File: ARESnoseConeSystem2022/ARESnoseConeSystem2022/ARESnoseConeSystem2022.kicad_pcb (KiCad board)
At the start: 2 copper layers, 125.2 x 66 mm, 36 parts, among them J1 436500200, J2 436500200, J3 BMP390_Headers, J4 ICM20948_Headers, J5 GPS_Headers1, J6 Transmitter_Headers1, J7 Conn_01x08, J8 Transmitter_Headers2, U1 L7805, U2 Teensy4.1

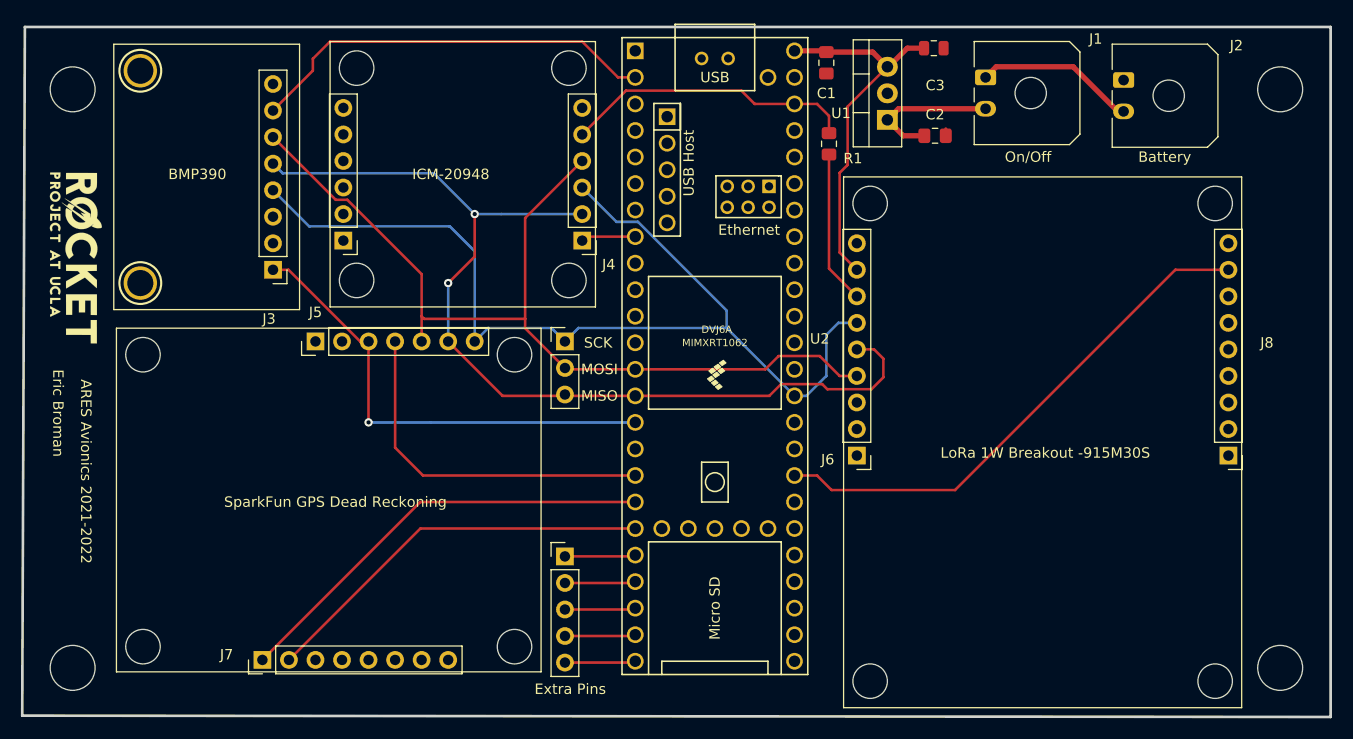
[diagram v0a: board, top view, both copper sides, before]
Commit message: Reworked Power & GND
New regulator + ground planes
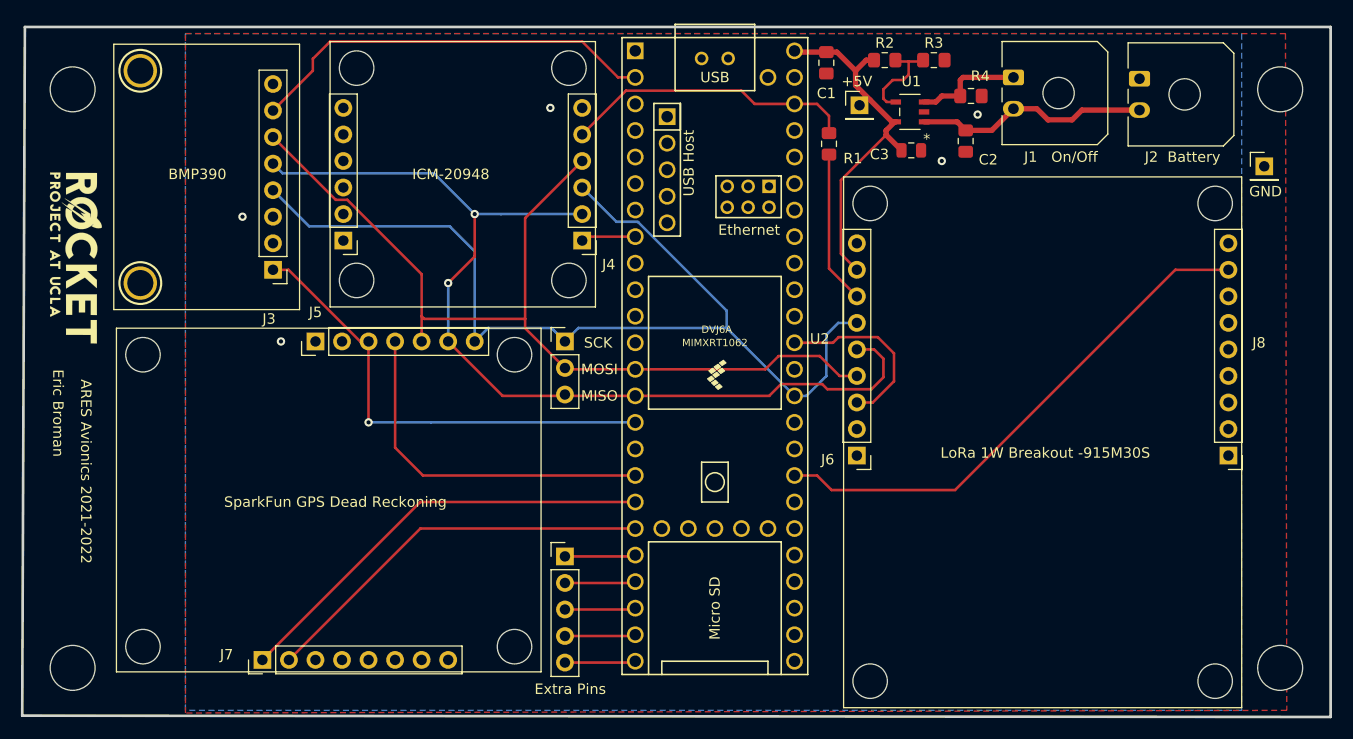
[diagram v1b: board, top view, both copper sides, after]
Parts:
- added +5V: PinHeader_1x01_P2.54mm_Vertical, Connector_PinHeader_2.54mm:PinHeader_1x01_P2.54mm_Vertical, F.Cu at (127.1, 53.7)
- added GND: PinHeader_1x01_P2.54mm_Vertical, Connector_PinHeader_2.54mm:PinHeader_1x01_P2.54mm_Vertical, F.Cu at (165.9, 59.6)
- added R2: 3 kOhm, Resistor_SMD:R_0805_2012Metric_Pad1.15x1.40mm_HandSolder, F.Cu at (129.5, 49.4)
- added R3: 9,1 kOhm, Resistor_SMD:R_0805_2012Metric_Pad1.15x1.40mm_HandSolder, F.Cu at (134.2, 49.4)
- added R4: 10 kOhm, Resistor_SMD:R_0805_2012Metric_Pad1.15x1.40mm_HandSolder, F.Cu at (137.8, 52.8)
- U1: value L7805 -> AP2210K-ADJTRG1; footprint Package_TO_SOT_THT:TO-220-3_Vertical -> footprints:AP2210K-ADJTRG1
- moved C3 10.0 mm to (132.1, 58.0)
- moved C2 2.97 mm to (137.3, 57.1), turned to 270 degrees
- moved J1 2.67 mm to (141.9, 51.1)
- moved U1 2.29 mm to (132.0, 54.4), turned to 180 degrees
- moved J2 1.53 mm to (153.9, 51.2)
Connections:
- C2 pad 1: Net-(C2-Pad1) -> +BATT
- J1 pad 2: Net-(C2-Pad1) -> +BATT
- J2 pad 2: Net-(J1-Pad1) -> +BATT
- U1 pad 1: Net-(C2-Pad1) -> +BATT
- U1 pad 3: 5V -> Net-(J1-Pad1)
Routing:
- net +BATT: track 0.00 -> 22.6 mm
- net /TRANSMITTER_CS: track 0.00 -> 17.5 mm
- net Net-(C2-Pad1): track 14.0 -> 0.00 mm
- net Net-(R2-Pad2): track 0.00 -> 9.22 mm
- net Net-(J1-Pad1): track 15.4 -> 10.4 mm
- net GND: track 0.70 -> 0.00 mm, vias 0 -> 5
- added copper zone on B.Cu, net GND
- added copper zone on F.Cu, net GND

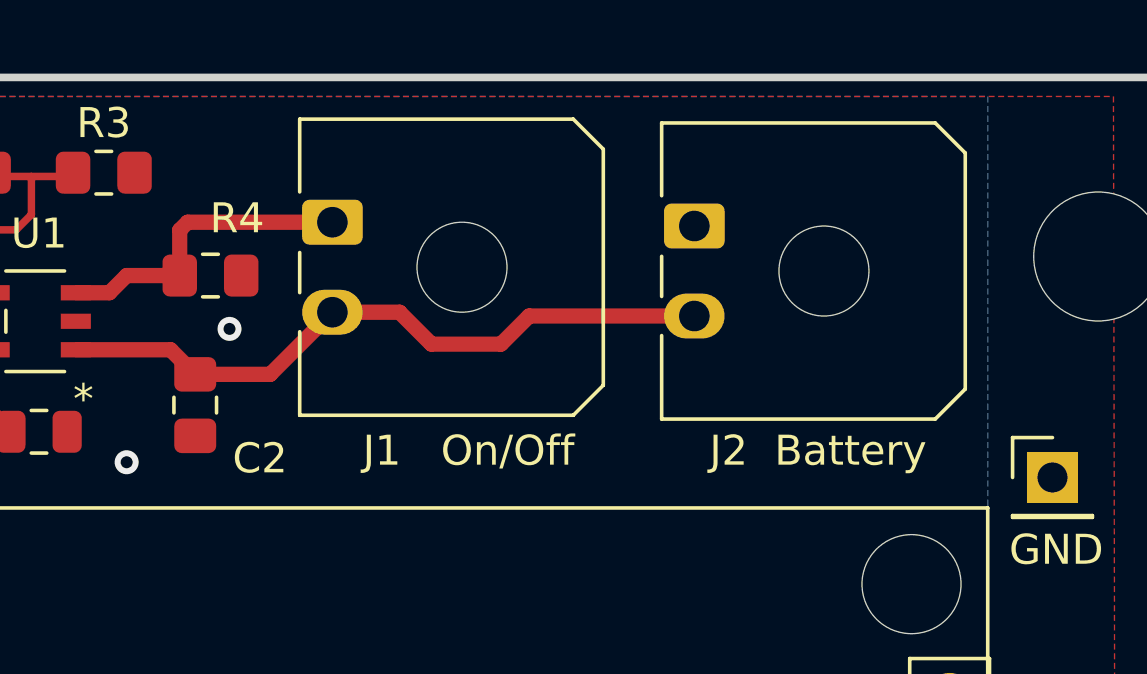
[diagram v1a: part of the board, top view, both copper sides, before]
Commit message: Fixed surface mount connectors
Reoriented since they are horizontal and not vertical
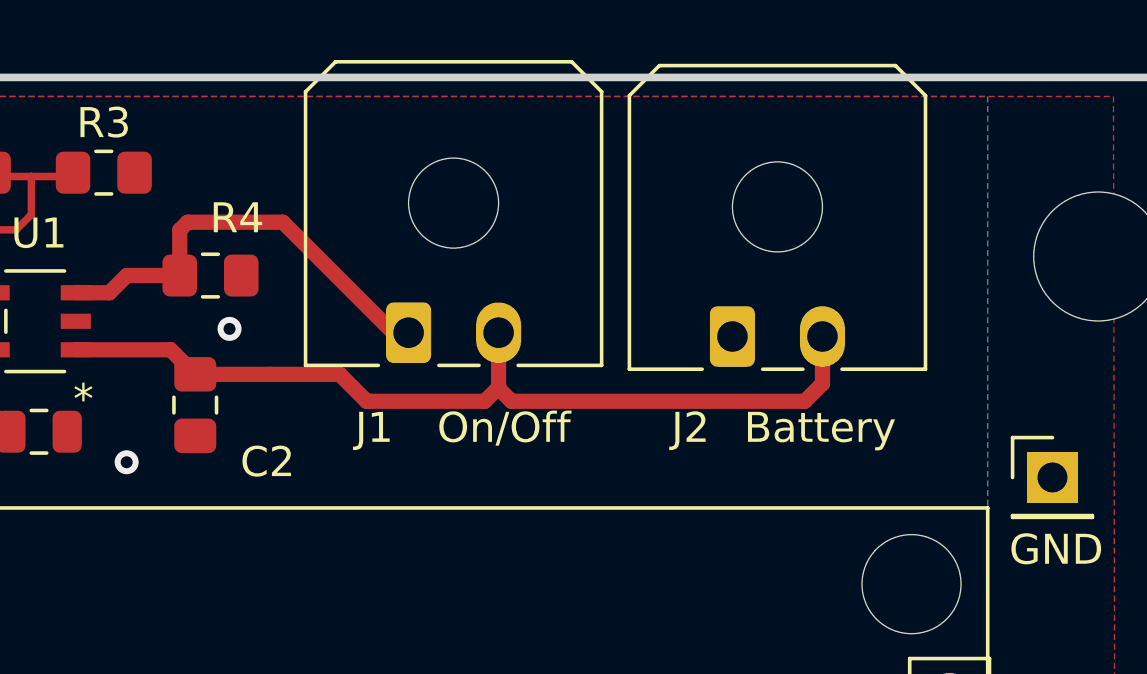
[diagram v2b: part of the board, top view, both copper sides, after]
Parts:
- moved J1 4.47 mm to (144.4, 54.7), turned to 0 degrees
- moved J2 3.90 mm to (155.2, 54.9), turned to 0 degrees
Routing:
- net +BATT: track 22.6 -> 29.6 mm
- net Net-(J1-Pad1): track 10.4 -> 14.5 mm

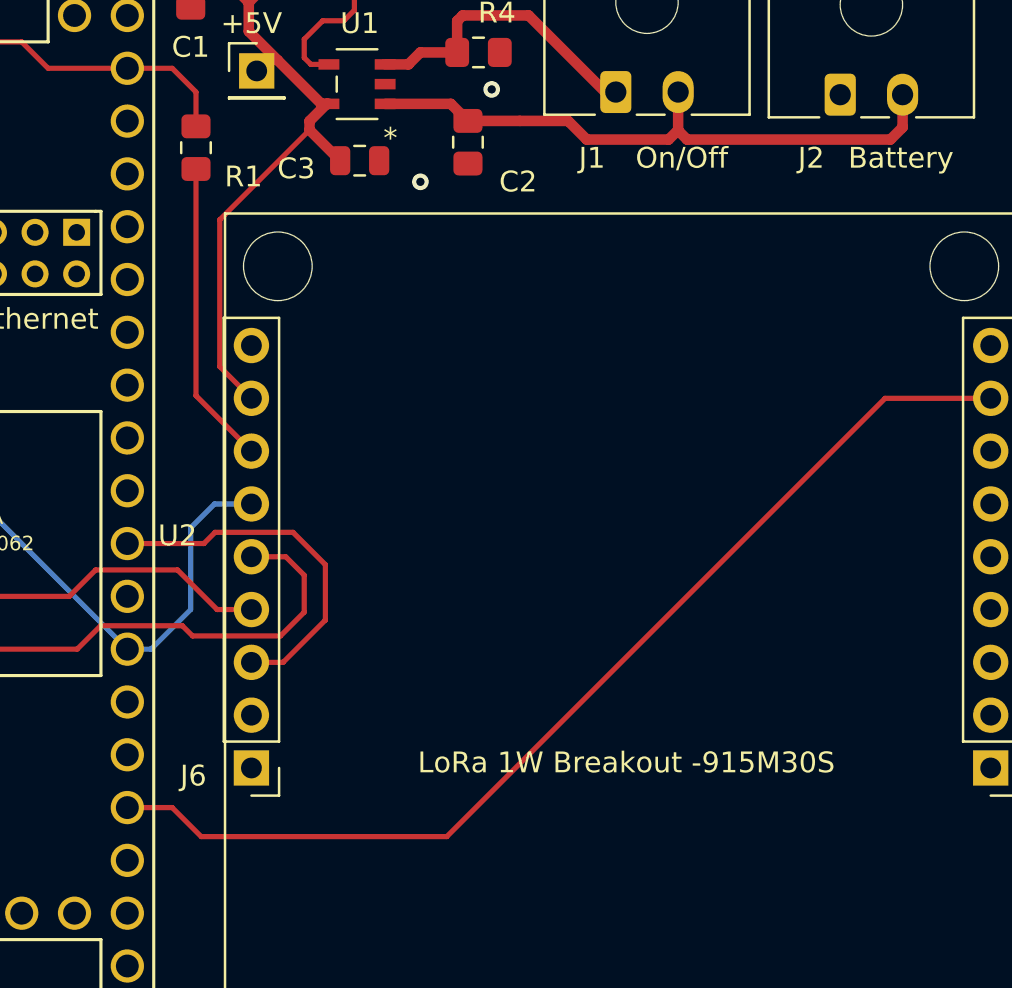
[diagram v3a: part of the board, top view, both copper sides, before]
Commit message: Added RXEN & TXEN pins on trasnceiver
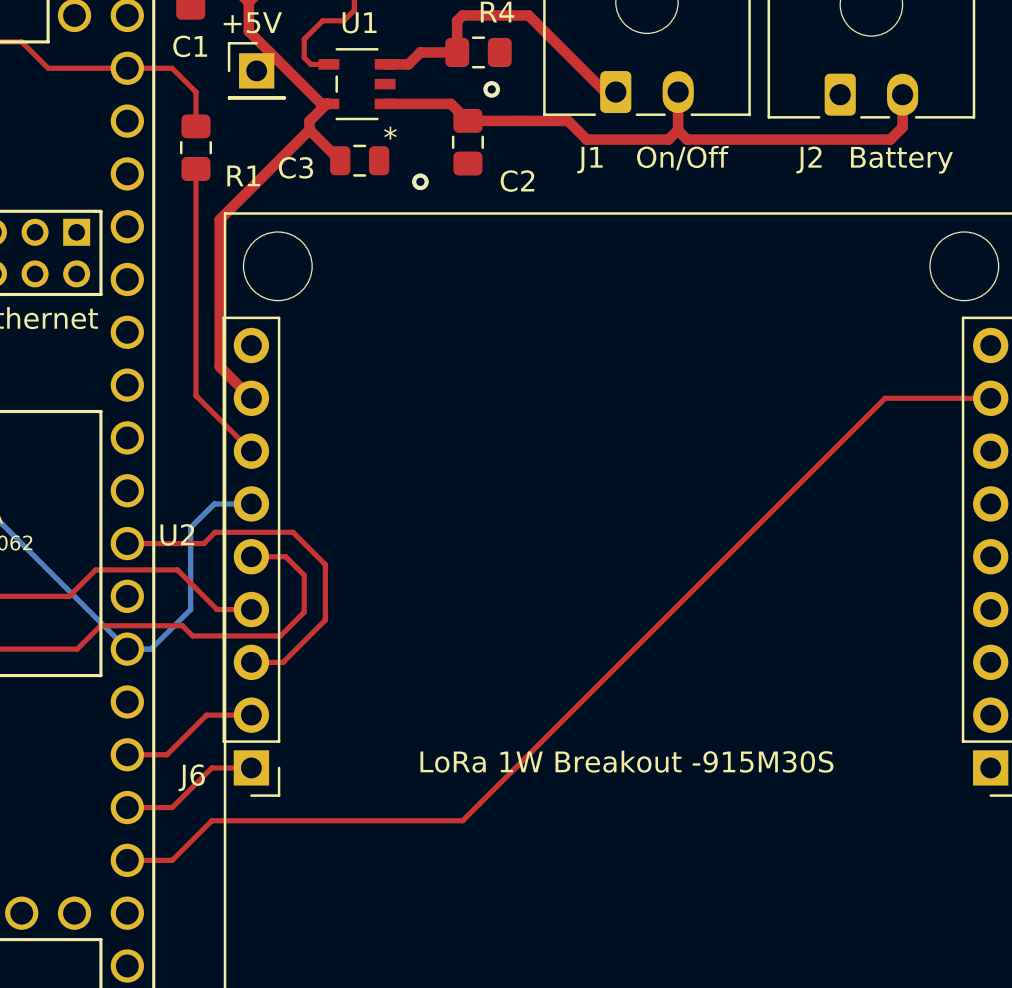
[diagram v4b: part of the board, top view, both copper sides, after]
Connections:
- J6 pad 1: Net-(J6-Pad1) -> /RXEN
- J6 pad 2: Net-(J6-Pad2) -> /TXEN
- U2 pad 31: Net-(U2-Pad31) -> /Transmitter_RST
- U2 pad 32: /Transmitter_RST -> /RXEN
- U2 pad 33: Net-(U2-Pad33) -> /TXEN
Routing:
- net /TXEN: track 0.00 -> 6.76 mm
- net /RXEN: track 0.00 -> 6.76 mm

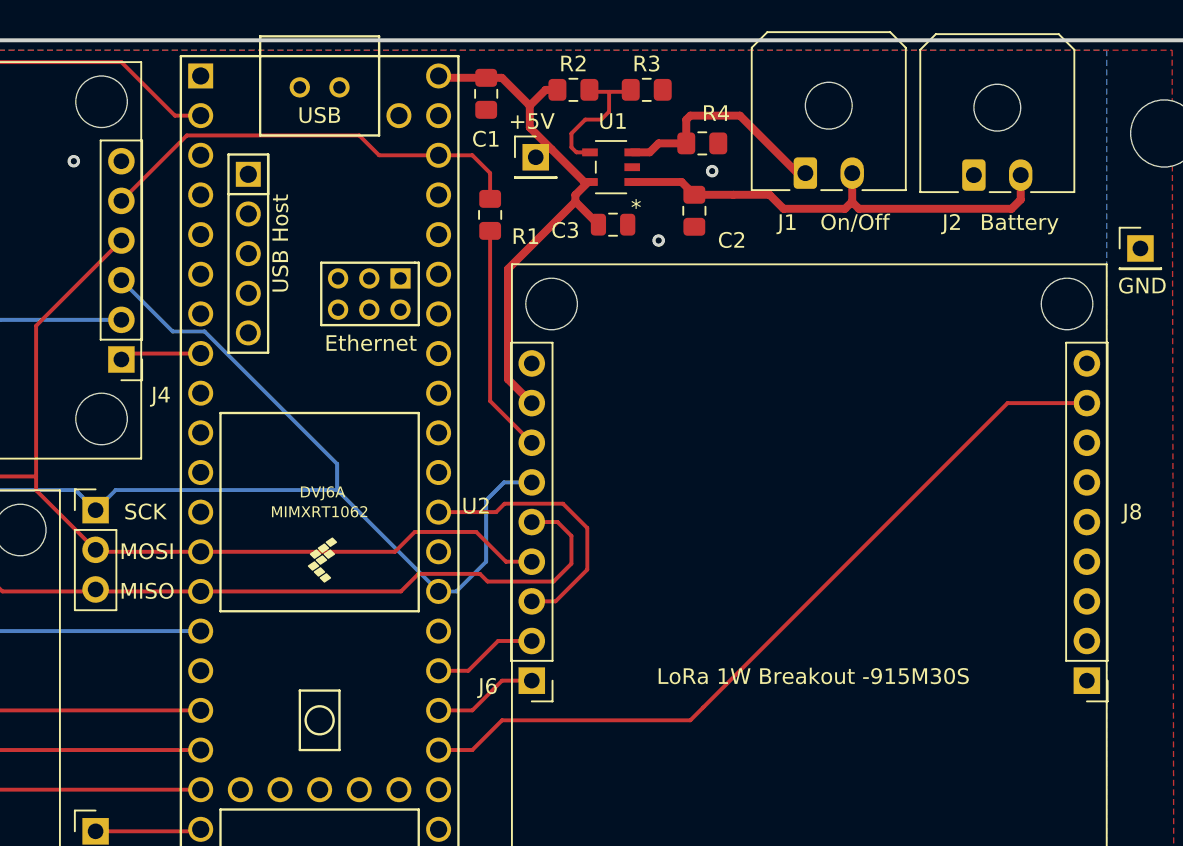
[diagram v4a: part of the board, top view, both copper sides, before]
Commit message: Upgrade power
1A LDO instead of 300 mA
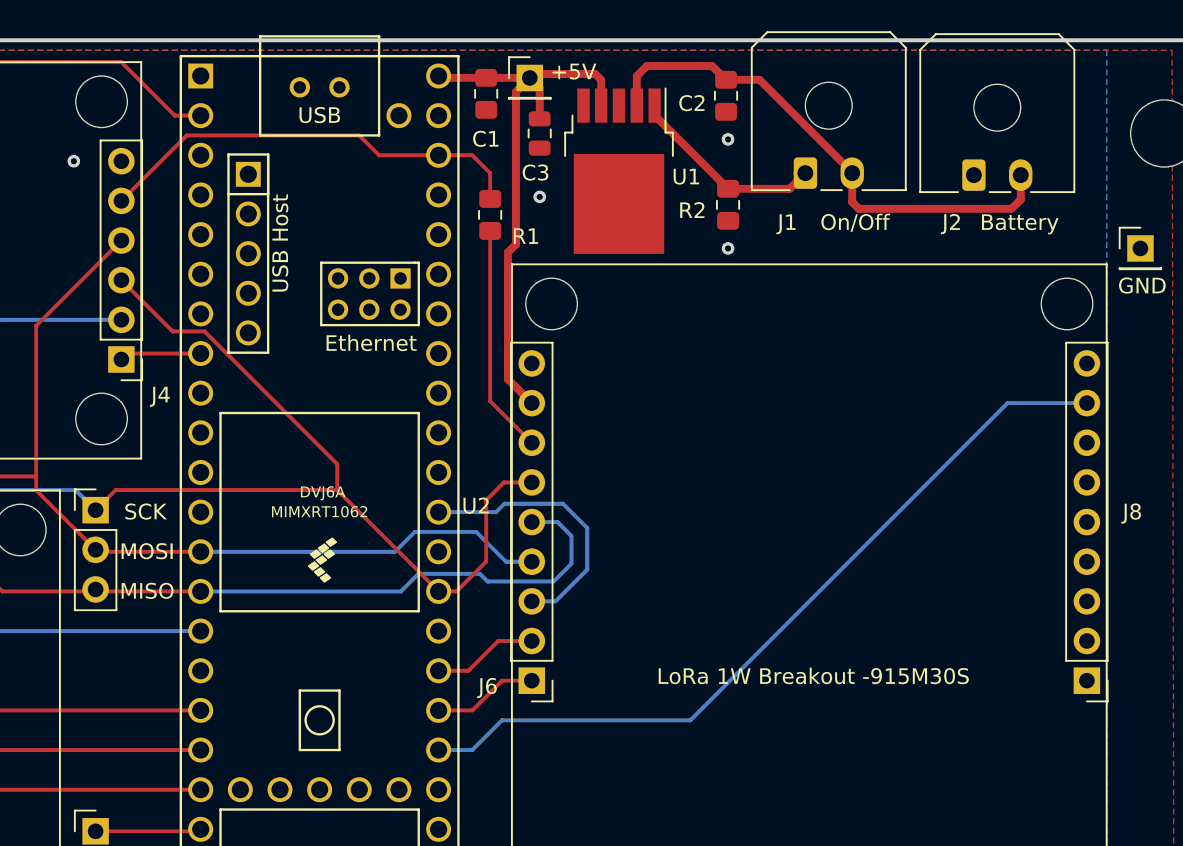
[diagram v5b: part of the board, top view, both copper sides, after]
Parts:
- removed the R2 at (129.5, 49.4)
- removed R3: 9,1 kOhm, Resistor_SMD:R_0805_2012Metric_Pad1.15x1.40mm_HandSolder
- U1: value AP2210K-ADJTRG1 -> BA05CC0WFP-E2; footprint footprints:AP2210K-ADJTRG1 -> Package_TO_SOT_SMD:TO-252-5_TabPin3
- moved C2 7.64 mm to (139.3, 49.8)
- moved C3 7.50 mm to (127.4, 52.2), turned to 270 degrees
- moved +5V 5.09 mm to (126.7, 48.6)
- moved R2 4.27 mm to (139.4, 56.8), turned to 270 degrees
- moved U1 0.57 mm to (132.5, 54.6), turned to 270 degrees
- renumbered R4 to R2
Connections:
- J8 pad 1: Net-(J8-Pad1) -> GND
- J8 pad 9: Net-(J8-Pad9) -> GND
- U1 pad 1: +BATT -> Net-(J1-Pad1)
- U1 pad 2: GND -> +BATT
- U1 pad 3: Net-(J1-Pad1) -> GND
- U1 pad 4: Net-(R2-Pad2) -> 5V
- U1 pad 5: 5V -> (no net)
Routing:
- net Net-(R2-Pad2): track 9.22 -> 0.00 mm
- net +BATT: track 29.6 -> 33.5 mm
- net Net-(J1-Pad1): track 14.5 -> 13.2 mm
- net 5V: track 36.0 -> 37.3 mm
- net GND: vias 5 -> 6
